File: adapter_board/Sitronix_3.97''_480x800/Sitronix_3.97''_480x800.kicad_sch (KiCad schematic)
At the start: 6 parts

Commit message: adapter_board.sitronix_3.97''_480x800: finish
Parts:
- J2: renamed from J?; footprint (none) -> Connector_FFC-FPC:Molex_502250-5191_2Rows-51Pins-1MP_P0.60mm_Horizontal
- J3: renamed from J?; footprint (none) -> Connector_PinHeader_2.54mm:PinHeader_1x03_P2.54mm_Vertical
- J4: renamed from J?; footprint (none) -> Connector_PinHeader_2.54mm:PinHeader_1x02_P2.54mm_Vertical
- R1, R2: renamed from R?; footprint (none) -> Resistor_SMD:R_0603_1608Metric
- gave numbers to parts that had none: 1
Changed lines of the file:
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@@
   (symbol (lib_id "Connector_Generic:Conn_02x26_Counter_Clockwise") (at 176.53 81.28 0) (mirror y) (unit 1)
     (in_bom yes) (on_board yes)
-    (property "Reference" "J?" (id 0) (at 173.99 48.26 0))
+    (property "Reference" "J2" (id 0) (at 179.07 48.26 0))
     (property "Value" "Conn_02x26_Counter_Clockwise" (id 1) (at 176.53 116.84 0))
-    (property "Footprint" "" (id 2) (at 176.53 81.28 0)
+    (property "Footprint" "Connector_FFC-FPC:Molex_502250-5191_2Rows-51Pins-1MP_P0.60mm_Horizontal" (id 2) (at 176.53 81.28 0)
       (effects (font (size 1.27 1.27)) hide)
     )
@@
   (symbol (lib_id "Connector_Others:ESP32-S3-LCD-EV-BOARD_SUB_LCD_RGB") (at 58.42 59.69 0) (unit 1)
     (in_bom yes) (on_board yes)
-    (property "Reference" "J?" (id 0) (at 59.69 58.42 0))
+    (property "Reference" "J1" (id 0) (at 59.69 58.42 0))
     (property "Value" "ESP32-S3-LCD-EV-BOARD_SUB_LCD_RGB" (id 1) (at 69.85 111.76 0))
     (property "Footprint" "Connector_PinSocket_2.54mm:PinSocket_2x20_P2.54mm_Vertical" (id 2) (at 72.39 115.57 0)
@@
   (symbol (lib_id "Connector_Generic:Conn_01x03") (at 201.93 55.88 0) (unit 1)
     (in_bom yes) (on_board yes) (fields_autoplaced)
-    (property "Reference" "J?" (id 0) (at 204.47 54.6099 0)
+    (property "Reference" "J3" (id 0) (at 204.47 54.6099 0)
       (effects (font (size 1.27 1.27)) (justify left))
     )
@@
       (effects (font (size 1.27 1.27)) (justify left))
     )
-    (property "Footprint" "" (id 2) (at 201.93 55.88 0)
+    (property "Footprint" "Connector_PinHeader_2.54mm:PinHeader_1x03_P2.54mm_Vertical" (id 2) (at 201.93 55.88 0)
       (effects (font (size 1.27 1.27)) hide)
     )
@@
   (symbol (lib_id "Connector_Generic:Conn_01x02") (at 201.93 66.04 0) (unit 1)
     (in_bom yes) (on_board yes) (fields_autoplaced)
-    (property "Reference" "J?" (id 0) (at 204.47 66.0399 0)
+    (property "Reference" "J4" (id 0) (at 204.47 66.0399 0)
       (effects (font (size 1.27 1.27)) (justify left))
     )
@@
       (effects (font (size 1.27 1.27)) (justify left))
     )
-    (property "Footprint" "" (id 2) (at 201.93 66.04 0)
+    (property "Footprint" "Connector_PinHeader_2.54mm:PinHeader_1x02_P2.54mm_Vertical" (id 2) (at 201.93 66.04 0)
       (effects (font (size 1.27 1.27)) hide)
     )
@@
   (symbol (lib_id "Device:R") (at 148.59 68.58 270) (unit 1)
     (in_bom yes) (on_board yes)
-    (property "Reference" "R?" (id 0) (at 146.05 71.12 90))
+    (property "Reference" "R1" (id 0) (at 147.32 71.12 90))
     (property "Value" "10K" (id 1) (at 147.32 66.04 90))
-    (property "Footprint" "" (id 2) (at 148.59 66.802 90)
+    (property "Footprint" "Resistor_SMD:R_0603_1608Metric" (id 2) (at 148.59 66.802 90)
       (effects (font (size 1.27 1.27)) hide)
     )
@@
   (symbol (lib_id "Device:R") (at 203.2 86.36 90) (unit 1)
     (in_bom yes) (on_board yes)
-    (property "Reference" "R?" (id 0) (at 205.74 83.82 90))
-    (property "Value" "10K" (id 1) (at 204.47 88.9 90))
-    (property "Footprint" "" (id 2) (at 203.2 88.138 90)
+    (property "Reference" "R2" (id 0) (at 201.93 88.9 90))
+    (property "Value" "10K" (id 1) (at 201.93 83.82 90))
+    (property "Footprint" "Resistor_SMD:R_0603_1608Metric" (id 2) (at 203.2 88.138 90)
       (effects (font (size 1.27 1.27)) hide)
     )
@@
   )
   (symbol_instances
+    (path "/2bb81e83-f098-496c-be23-3549cca0c92e"
+      (reference "J1") (unit 1) (value "ESP32-S3-LCD-EV-BOARD_SUB_LCD_RGB") (footprint "Connector_PinSocket_2.54mm:PinSocket_2x20_P2.54mm_Vertical")
+    )
     (path "/15c8599b-a833-4656-82c4-0f3fd7902e2f"
-      (reference "J?") (unit 1) (value "Conn_02x26_Counter_Clockwise") (footprint "")
-    )
-    (path "/2bb81e83-f098-496c-be23-3549cca0c92e"
-      (reference "J?") (unit 1) (value "ESP32-S3-LCD-EV-BOARD_SUB_LCD_RGB") (footprint "Connector_PinSocket_2.54mm:PinSocket_2x20_P2.54mm_Vertical")
+      (reference "J2") (unit 1) (value "Conn_02x26_Counter_Clockwise") (footprint "Connector_FFC-FPC:Molex_502250-5191_2Rows-51Pins-1MP_P0.60mm_Horizontal")
     )
     (path "/5c44bb0a-3445-4361-8d12-6812880d5f2e"
-      (reference "J?") (unit 1) (value "Conn_01x03") (footprint "")
+      (reference "J3") (unit 1) (value "Conn_01x03") (footprint "Connector_PinHeader_2.54mm:PinHeader_1x03_P2.54mm_Vertical")
     )
     (path "/62f5ad86-1633-4260-9594-a601b691991e"
-      (reference "J?") (unit 1) (value "Conn_01x02") (footprint "")
+      (reference "J4") (unit 1) (value "Conn_01x02") (footprint "Connector_PinHeader_2.54mm:PinHeader_1x02_P2.54mm_Vertical")
     )
     (path "/ce954d38-388e-40ba-97de-1684b9be998f"
-      (reference "R?") (unit 1) (value "10K") (footprint "")
+      (reference "R1") (unit 1) (value "10K") (footprint "Resistor_SMD:R_0603_1608Metric")
     )
     (path "/e99a7932-cf29-404c-a5c0-f2e26a90cbbf"
-      (reference "R?") (unit 1) (value "10K") (footprint "")
+      (reference "R2") (unit 1) (value "10K") (footprint "Resistor_SMD:R_0603_1608Metric")
     )
   )

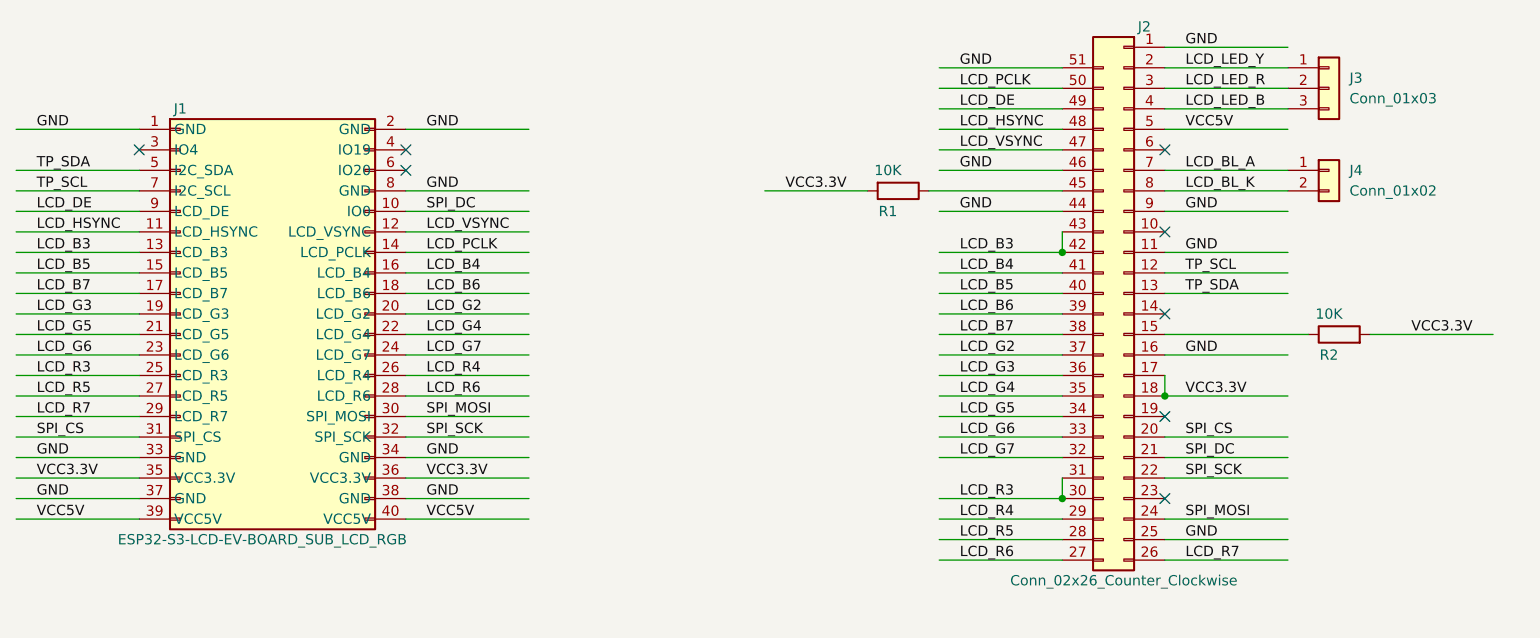
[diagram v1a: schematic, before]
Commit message: adapter_board.sitronix_3.97''_800x480: modify
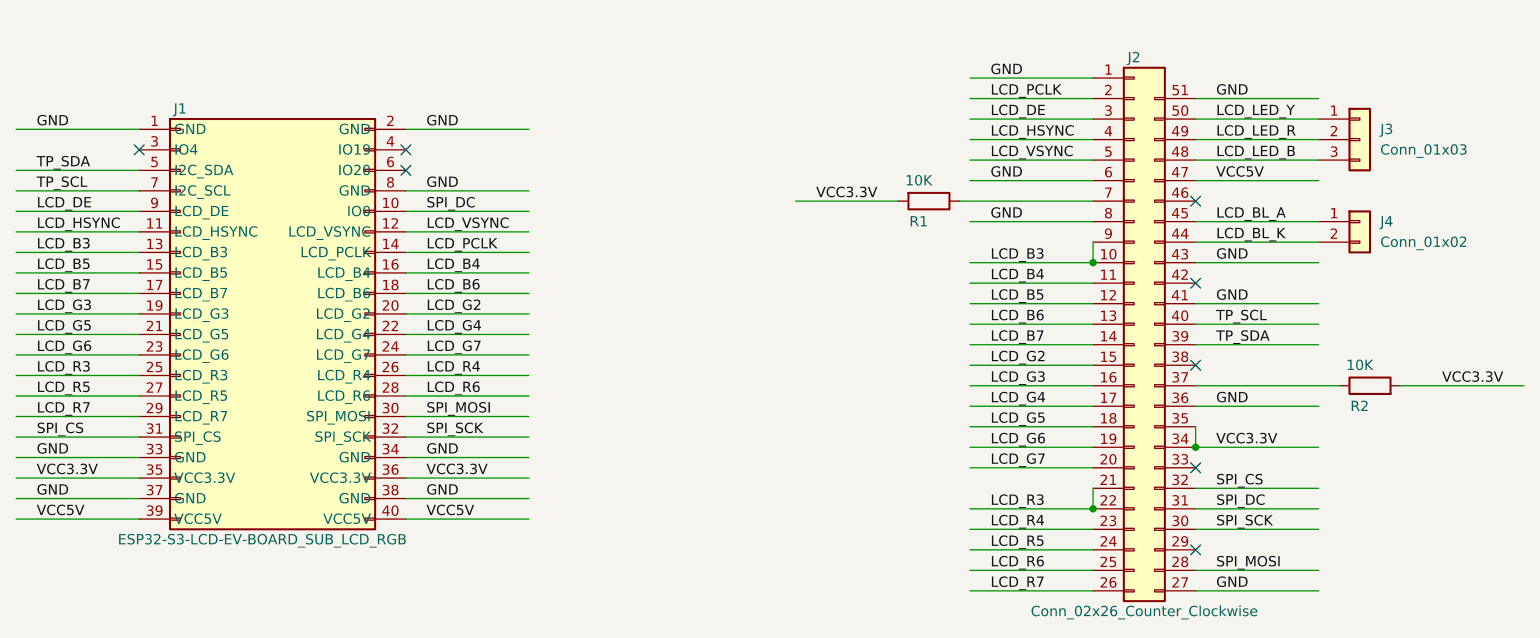
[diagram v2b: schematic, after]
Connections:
- net GND: now also J2.27 (Pin_27), J2.36 (Pin_36), J2.41 (Pin_41), J2.43 (Pin_43), J2.6 (Pin_6), J2.8 (Pin_8); no longer J2.11 (Pin_11), J2.16 (Pin_16), J2.25 (Pin_25), J2.44 (Pin_44), J2.46 (Pin_46), J2.9 (Pin_9)
- net LCD_B3: now also J2.10 (Pin_10), J2.9 (Pin_9); no longer J2.42 (Pin_42), J2.43 (Pin_43)
- net LCD_B4: now also J2.11 (Pin_11); no longer J2.41 (Pin_41)
- net LCD_B5: now also J2.12 (Pin_12); no longer J2.40 (Pin_40)
- net LCD_B6: now also J2.13 (Pin_13); no longer J2.39 (Pin_39)
- net LCD_B7: now also J2.14 (Pin_14); no longer J2.38 (Pin_38)
- net LCD_BL_A: now also J2.45 (Pin_45); no longer J2.7 (Pin_7)
- net LCD_BL_K: now also J2.44 (Pin_44); no longer J2.8 (Pin_8)
- net LCD_DE: now also J2.3 (Pin_3); no longer J2.49 (Pin_49)
- net LCD_G2: now also J2.15 (Pin_15); no longer J2.37 (Pin_37)
- net LCD_G3: now also J2.16 (Pin_16); no longer J2.36 (Pin_36)
- net LCD_G4: now also J2.17 (Pin_17); no longer J2.35 (Pin_35)
- net LCD_G5: now also J2.18 (Pin_18); no longer J2.34 (Pin_34)
- net LCD_G6: now also J2.19 (Pin_19); no longer J2.33 (Pin_33)
- net LCD_G7: now also J2.20 (Pin_20); no longer J2.32 (Pin_32)
- net LCD_HSYNC: now also J2.4 (Pin_4); no longer J2.48 (Pin_48)
- net LCD_LED_B: now also J2.48 (Pin_48); no longer J2.4 (Pin_4)
- net LCD_LED_R: now also J2.49 (Pin_49); no longer J2.3 (Pin_3)
- net LCD_LED_Y: now also J2.50 (Pin_50); no longer J2.2 (Pin_2)
- net LCD_PCLK: now also J2.2 (Pin_2); no longer J2.50 (Pin_50)
- net LCD_R3: now also J2.21 (Pin_21), J2.22 (Pin_22); no longer J2.30 (Pin_30), J2.31 (Pin_31)
- net LCD_R4: now also J2.23 (Pin_23); no longer J2.29 (Pin_29)
- net LCD_R5: now also J2.24 (Pin_24); no longer J2.28 (Pin_28)
- net LCD_R6: now also J2.25 (Pin_25); no longer J2.27 (Pin_27)
- net LCD_VSYNC: now also J2.5 (Pin_5); no longer J2.47 (Pin_47)
- net SPI_CS: now also J2.32 (Pin_32); no longer J2.20 (Pin_20)
- net SPI_DC: now also J2.31 (Pin_31); no longer J2.21 (Pin_21)
- net SPI_MOSI: now also J2.28 (Pin_28); no longer J2.24 (Pin_24)
- net SPI_SCK: now also J2.30 (Pin_30); no longer J2.22 (Pin_22)
- net TP_SCL: now also J2.40 (Pin_40); no longer J2.12 (Pin_12)
- net TP_SDA: now also J2.39 (Pin_39); no longer J2.13 (Pin_13)
- net VCC3.3V: now also J2.34 (Pin_34), J2.35 (Pin_35); no longer J2.17 (Pin_17), J2.18 (Pin_18)
- net VCC5V: now also J2.47 (Pin_47); no longer J2.5 (Pin_5)
- net at R2.1: now also J2.37 (Pin_37); no longer J2.15 (Pin_15)
- net at R1.1: now also J2.7 (Pin_7); no longer J2.45 (Pin_45)
